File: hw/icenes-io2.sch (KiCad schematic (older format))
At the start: 35 parts, among them J4 Conn_02x31_Odd_Even, J5 Conn_02x31_Odd_Even, U4 iCE40HX8K-CT256, X2 DSC1001BI2-133.0000T

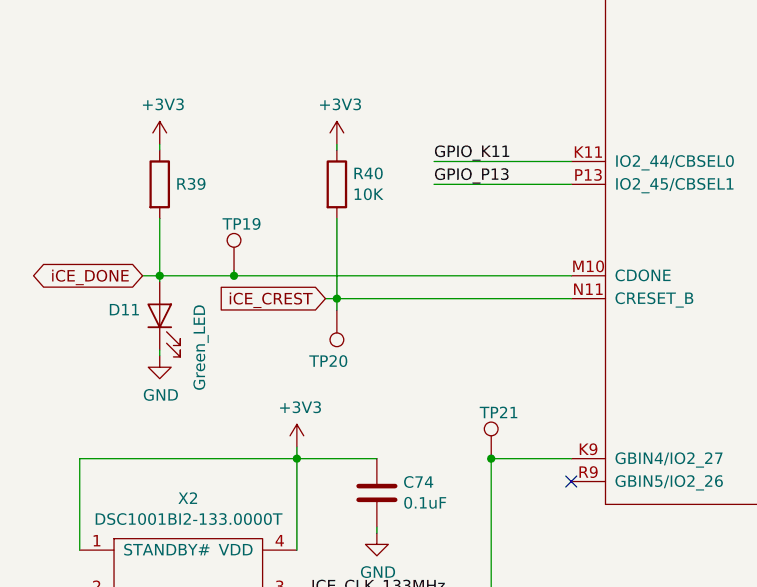
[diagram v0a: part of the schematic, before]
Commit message: Added voltage range in Vin lable (+5V to +10V).
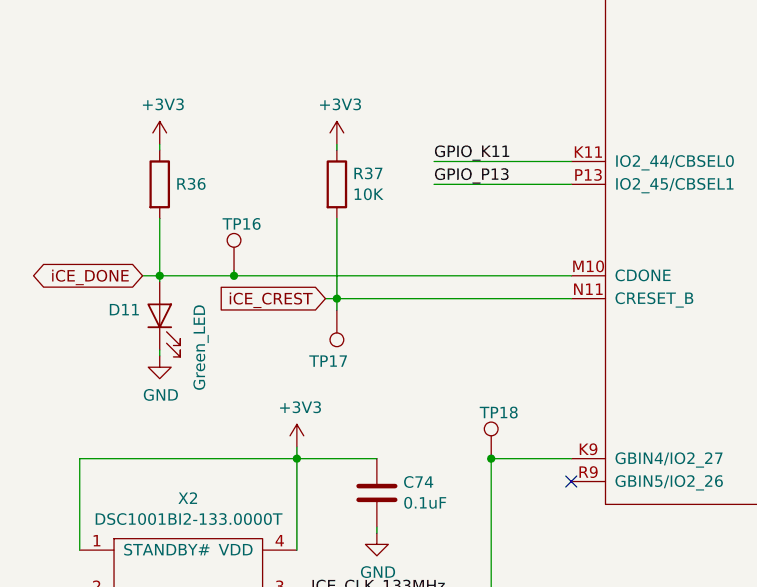
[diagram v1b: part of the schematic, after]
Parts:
- renumbered R39 to R36, R40 to R37, TP19 to TP16, TP20 to TP17, TP21 to TP18
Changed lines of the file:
@@
 $EndComp
 $Comp
-L icenes-library:R10K R40
+L icenes-library:R10K R37
 U 1 1 5D1F5A80
 P 2075 4200
-F 0 "R40" V 2029 4270 50  0000 L CNN
+F 0 "R37" V 2029 4270 50  0000 L CNN
 F 1 "R10K" H 2075 4100 50  0001 C CNN
 F 2 "Resistor_SMD:R_0603_1608Metric_Pad1.05x0.95mm_HandSolder" V 2075 4200 50  0001 C CNN
@@
 NoConn ~ 9850 6300
 $Comp
-L icenes-library:R_TBD R39
+L icenes-library:R_TBD R36
 U 1 1 5DA26BEC
 P 1300 4200
-F 0 "R39" V 1300 4270 50  0000 L CNN
+F 0 "R36" V 1300 4270 50  0000 L CNN
 F 1 "R_TBD" H 1300 4100 50  0001 C CNN
 F 2 "Resistor_SMD:R_0603_1608Metric_Pad1.05x0.95mm_HandSolder" V 1300 4200 50  0001 C CNN
@@
 	1300 4350 1300 4600
 $Comp
-L icenes-library:TestPoint TP20
+L icenes-library:TestPoint TP17
 U 1 1 5DCF35FF
 P 2075 4750
-F 0 "TP20" H 2025 4975 50  0000 L CNN
+F 0 "TP17" H 2025 4975 50  0000 L CNN
 F 1 "TestPoint" H 2075 4950 50  0001 C CNN
 F 2 "TestPoint:TestPoint_Pad_D1.0mm" H 2275 4750 50  0001 C CNN
@@
 	2250 5725 2250 5700
 $Comp
-L icenes-library:TestPoint TP21
+L icenes-library:TestPoint TP18
 U 1 1 5DDBB4BD
 P 2750 5400
-F 0 "TP21" H 2700 5600 50  0000 L CNN
+F 0 "TP18" H 2700 5600 50  0000 L CNN
 F 1 "TestPoint" H 2750 5600 50  0001 C CNN
 F 2 "TestPoint:TestPoint_Pad_D1.0mm" H 2950 5400 50  0001 C CNN
@@
 $EndComp
 $Comp
-L icenes-library:TestPoint TP19
+L icenes-library:TestPoint TP16
 U 1 1 5DDC0B2C
 P 1625 4575
-F 0 "TP19" H 1575 4775 50  0000 L CNN
+F 0 "TP16" H 1575 4775 50  0000 L CNN
 F 1 "TestPoint" H 1625 4775 50  0001 C CNN
 F 2 "TestPoint:TestPoint_Pad_D1.0mm" H 1825 4575 50  0001 C CNN

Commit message: Rough board layout.
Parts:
- added R38: R0_0603, Resistor_SMD:R_0603_1608Metric_Pad1.05x0.95mm_HandSolder, symbol icenes-library:R0_0603
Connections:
- net iCE_DONE: now also R38.1; no longer D11.2 (A)
- new net: D11.2 (A), R38.2
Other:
- moved on the sheet: C74, D11, X2
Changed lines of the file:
@@
 L icenes-library:Green_LED D11
 U 1 1 5DA2730F
-P 1300 4775
-F 0 "D11" V 1325 5000 50  0000 R CNN
-F 1 "Green_LED" H 1350 4600 50  0000 R CNN
-F 2 "LED_SMD:LED_0805_2012Metric_Pad1.15x1.40mm_HandSolder" H 1300 4775 50  0001 C CNN
-F 3 "https://www.mouser.se/datasheet/2/216/APTD2012LCGCK-1102037.pdf" H 1300 4775 50  0001 C CNN
-F 4 "Kingbright" H 1300 4775 50  0001 C CNN "Manufacturer"
-F 5 "APTD2012LCGCK" H 1300 4775 50  0001 C CNN "Part number"
-	1    1300 4775
+P 1300 5100
+F 0 "D11" V 1325 5325 50  0000 R CNN
+F 1 "Green_LED" H 1350 4925 50  0000 R CNN
+F 2 "LED_SMD:LED_0805_2012Metric_Pad1.15x1.40mm_HandSolder" H 1300 5100 50  0001 C CNN
+F 3 "https://www.mouser.se/datasheet/2/216/APTD2012LCGCK-1102037.pdf" H 1300 5100 50  0001 C CNN
+F 4 "Kingbright" H 1300 5100 50  0001 C CNN "Manufacturer"
+F 5 "APTD2012LCGCK" H 1300 5100 50  0001 C CNN "Part number"
+	1    1300 5100
 	0    -1   -1   0
 $EndComp
@@
 L power:GND #PWR?
 U 1 1 5DA5244F
-P 1300 4950
+P 1300 5275
 AR Path="/5D1BB1FB/5DA5244F" Ref="#PWR?"  Part="1"
 AR Path="/5D1BB49B/5DA5244F" Ref="#PWR090"  Part="1"
-F 0 "#PWR090" H 1300 4700 50  0001 C CNN
-F 1 "GND" H 1305 4777 50  0000 C CNN
-F 2 "" H 1300 4950 50  0001 C CNN
-F 3 "" H 1300 4950 50  0001 C CNN
-	1    1300 4950
+F 0 "#PWR090" H 1300 5025 50  0001 C CNN
+F 1 "GND" H 1305 5102 50  0000 C CNN
+F 2 "" H 1300 5275 50  0001 C CNN
+F 3 "" H 1300 5275 50  0001 C CNN
+	1    1300 5275
 	1    0    0    -1
 $EndComp
@@
 	1300 4025 1300 4050
 Wire Wire Line
-	1300 4925 1300 4950
+	1300 5250 1300 5275
 Wire Wire Line
 	1225 4600 1300 4600
@@
 L icenes-library:C0.1uF C?
 U 1 1 5DC56E81
-P 2250 5550
+P 2250 5650
 AR Path="/5D1BAC88/5DC56E81" Ref="C?"  Part="1"
 AR Path="/5D1BB49B/5DC56E81" Ref="C74"  Part="1"
-F 0 "C74" H 2365 5596 50  0000 L CNN
-F 1 "C0.1uF" H 2100 5450 50  0001 C CNN
-F 2 "Capacitor_SMD:C_0603_1608Metric_Pad1.05x0.95mm_HandSolder" H 2250 5550 50  0001 C CNN
-F 3 "https://www.mouser.se/datasheet/2/445/885012206020-554242.pdf" H 2250 5550 50  0001 C CNN
-F 4 "0.1uF" H 2365 5505 50  0000 L CNN "Capacitance"
-F 5 "Wurth" H 2250 5550 50  0001 C CNN "Manufacturer"
-F 6 "885012206020 " H 2250 5550 50  0001 C CNN "Part number"
-	1    2250 5550
+F 0 "C74" H 2365 5696 50  0000 L CNN
+F 1 "C0.1uF" H 2100 5550 50  0001 C CNN
+F 2 "Capacitor_SMD:C_0603_1608Metric_Pad1.05x0.95mm_HandSolder" H 2250 5650 50  0001 C CNN
+F 3 "https://www.mouser.se/datasheet/2/445/885012206020-554242.pdf" H 2250 5650 50  0001 C CNN
+F 4 "0.1uF" H 2365 5605 50  0000 L CNN "Capacitance"
+F 5 "Wurth" H 2250 5650 50  0001 C CNN "Manufacturer"
+F 6 "885012206020 " H 2250 5650 50  0001 C CNN "Part number"
+	1    2250 5650
 	1    0    0    -1
 $EndComp
@@
 L power:GND #PWR?
 U 1 1 5DC56E8F
-P 2250 5725
+P 2250 5825
 AR Path="/5D1BAC88/5DC56E8F" Ref="#PWR?"  Part="1"
 AR Path="/5D1BB49B/5DC56E8F" Ref="#PWR0104"  Part="1"
-F 0 "#PWR0104" H 2250 5475 50  0001 C CNN
-F 1 "GND" H 2255 5552 50  0000 C CNN
-F 2 "" H 2250 5725 50  0001 C CNN
-F 3 "" H 2250 5725 50  0001 C CNN
-	1    2250 5725
-	1    0    0    -1
-$EndComp
-Wire Wire Line
-	1900 5400 2250 5400
-Wire Wire Line
-	1900 5400 1900 5800
-Wire Wire Line
-	1900 5350 1900 5400
-Connection ~ 1900 5400
-Wire Wire Line
-	950  5800 950  5400
-Wire Wire Line
-	950  5400 1900 5400
+F 0 "#PWR0104" H 2250 5575 50  0001 C CNN
+F 1 "GND" H 2255 5652 50  0000 C CNN
+F 2 "" H 2250 5825 50  0001 C CNN
+F 3 "" H 2250 5825 50  0001 C CNN
+	1    2250 5825
+	1    0    0    -1
+$EndComp
+Wire Wire Line
+	1900 5500 2250 5500
+Wire Wire Line
+	1900 5500 1900 5900
+Wire Wire Line
+	1900 5450 1900 5500
+Connection ~ 1900 5500
+Wire Wire Line
+	950  5900 950  5500
+Wire Wire Line
+	950  5500 1900 5500
 $Comp
 L power:GND #PWR?
 U 1 1 5DC56E9C
-P 950 6100
+P 950 6200
 AR Path="/5D1BAC88/5DC56E9C" Ref="#PWR?"  Part="1"
 AR Path="/5D1BB49B/5DC56E9C" Ref="#PWR087"  Part="1"
-F 0 "#PWR087" H 950 5850 50  0001 C CNN
-F 1 "GND" H 955 5927 50  0000 C CNN
-F 2 "" H 950 6100 50  0001 C CNN
-F 3 "" H 950 6100 50  0001 C CNN
-	1    950  6100
-	1    0    0    -1
-$EndComp
-Wire Wire Line
-	950  6000 950  6100
-Wire Wire Line
-	1900 6000 2750 6000
+F 0 "#PWR087" H 950 5950 50  0001 C CNN
+F 1 "GND" H 955 6027 50  0000 C CNN
+F 2 "" H 950 6200 50  0001 C CNN
+F 3 "" H 950 6200 50  0001 C CNN
+	1    950  6200
+	1    0    0    -1
+$EndComp
+Wire Wire Line
+	950  6100 950  6200
+Wire Wire Line
+	1900 6100 2750 6100
 $Comp
 L icenes-library:DSC1001BI2-133.0000T X2
 U 1 1 5DCE10E2
-P 1450 5700
-F 0 "X2" H 1425 5825 50  0000 C CNN
-F 1 "DSC1001BI2-133.0000T" H 1425 5734 50  0000 C CNN
-F 2 "icenes-library:MEMS_Microship_Ocillator_SMD_CDFN-4_5.0x3.2mm" H 1550 5750 50  0001 C CNN
-F 3 "https://ww1.microchip.com/downloads/en/DeviceDoc/20005529B.pdf" H 1550 5750 50  0001 C CNN
-F 4 "Microchip" H 1450 5700 50  0001 C CNN "Manufacturer"
-F 5 "DSC1001BI2-133.0000T" H 1450 5700 50  0001 C CNN "Part number"
-	1    1450 5700
-	1    0    0    -1
-$EndComp
-Wire Wire Line
-	2750 6000 2750 5400
+P 1450 5800
+F 0 "X2" H 1425 5925 50  0000 C CNN
+F 1 "DSC1001BI2-133.0000T" H 1425 5834 50  0000 C CNN
+F 2 "icenes-library:MEMS_Microship_Ocillator_SMD_CDFN-4_5.0x3.2mm" H 1550 5850 50  0001 C CNN
+F 3 "https://ww1.microchip.com/downloads/en/DeviceDoc/20005529B.pdf" H 1550 5850 50  0001 C CNN
+F 4 "Microchip" H 1450 5800 50  0001 C CNN "Manufacturer"
+F 5 "DSC1001BI2-133.0000T" H 1450 5800 50  0001 C CNN "Part number"
+	1    1450 5800
+	1    0    0    -1
+$EndComp
 Wire Wire Line
 	2750 5400 3100 5400
 NoConn ~ 3100 5500
-Text Label 2550 6000 2    50   ~ 0
+Text Label 2550 6100 2    50   ~ 0
 ICE_CLK_133MHz
 Wire Wire Line
-	2250 5725 2250 5700
+	2250 5825 2250 5800
 $Comp
 L icenes-library:TestPoint TP18
@@
 L power:+3V3 #PWR095
 U 1 1 5DDBDDE4
-P 1900 5350
-F 0 "#PWR095" H 1900 5200 50  0001 C CNN
-F 1 "+3V3" H 1915 5523 50  0000 C CNN
-F 2 "" H 1900 5350 50  0001 C CNN
-F 3 "" H 1900 5350 50  0001 C CNN
-	1    1900 5350
+P 1900 5450
+F 0 "#PWR095" H 1900 5300 50  0001 C CNN
+F 1 "+3V3" H 1915 5623 50  0000 C CNN
+F 2 "" H 1900 5450 50  0001 C CNN
+F 3 "" H 1900 5450 50  0001 C CNN
+	1    1900 5450
 	1    0    0    -1
 $EndComp
@@
 Wire Wire Line
 	2550 3000 2550 3050
+$Comp
+L icenes-library:R0_0603 R38
+U 1 1 5DCDC52E
+P 1300 4775
+F 0 "R38" V 1254 4845 50  0000 L CNN
+F 1 "R0_0603" H 1300 4675 50  0001 C CNN
+F 2 "Resistor_SMD:R_0603_1608Metric_Pad1.05x0.95mm_HandSolder" V 1300 4775 50  0001 C CNN
+F 3 "https://www.mouser.se/datasheet/2/447/PYu-RC_Group_51_RoHS_L_10-1527934.pdf" V 1300 4775 50  0001 C CNN
+F 4 "0" V 1345 4845 50  0000 L CNN "Resistance"
+F 5 "Yageo" H 1300 4775 50  0001 C CNN "Manufacturer"
+F 6 "RC0603FR-070RL" H 1300 4775 50  0001 C CNN "Part number"
+	1    1300 4775
+	0    1    1    0
+$EndComp
+Wire Wire Line
+	1300 4925 1300 4950
+Wire Wire Line
+	2750 5400 2750 6100
 $EndSCHEMATC

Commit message: Layout.
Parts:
- removed C74: C0.1uF, Capacitor_SMD:C_0603_1608Metric_Pad1.05x0.95mm_HandSolder, symbol icenes-library:C0.1uF
- removed D11: Green_LED, LED_SMD:LED_0805_2012Metric_Pad1.15x1.40mm_HandSolder, symbol icenes-library:Green_LED
- removed R38: R0_0603, Resistor_SMD:R_0603_1608Metric_Pad1.05x0.95mm_HandSolder, symbol icenes-library:R0_0603
- removed TP18: TestPoint, TestPoint:TestPoint_Pad_D1.0mm, symbol icenes-library:TestPoint
- removed X2: DSC1001BI2-133.0000T, icenes-library:MEMS_Microship_Ocillator_SMD_CDFN-4_5.0x3.2mm, symbol icenes-library:DSC1001BI2-133.0000T
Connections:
- net ICE_CLK_133MHz: no longer names the net of U4.K9 (GBIN4/IO2_27)
- no-connect marks 2 -> 3
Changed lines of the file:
@@
-$EndComp
-$Comp
-L icenes-library:Green_LED D11
-U 1 1 5DA2730F
-P 1300 5100
-F 0 "D11" V 1325 5325 50  0000 R CNN
-F 1 "Green_LED" H 1350 4925 50  0000 R CNN
-F 2 "LED_SMD:LED_0805_2012Metric_Pad1.15x1.40mm_HandSolder" H 1300 5100 50  0001 C CNN
-F 3 "https://www.mouser.se/datasheet/2/216/APTD2012LCGCK-1102037.pdf" H 1300 5100 50  0001 C CNN
-F 4 "Kingbright" H 1300 5100 50  0001 C CNN "Manufacturer"
-F 5 "APTD2012LCGCK" H 1300 5100 50  0001 C CNN "Part number"
-	1    1300 5100
-	0    -1   -1   0
 $EndComp
 $Comp
@@
 	1    0    0    -1
 $EndComp
-$Comp
-L power:GND #PWR?
-U 1 1 5DA5244F
-P 1300 5275
-AR Path="/5D1BB1FB/5DA5244F" Ref="#PWR?"  Part="1"
-AR Path="/5D1BB49B/5DA5244F" Ref="#PWR090"  Part="1"
-F 0 "#PWR090" H 1300 5025 50  0001 C CNN
-F 1 "GND" H 1305 5102 50  0000 C CNN
-F 2 "" H 1300 5275 50  0001 C CNN
-F 3 "" H 1300 5275 50  0001 C CNN
-	1    1300 5275
-	1    0    0    -1
-$EndComp
 Wire Wire Line
 	1300 4025 1300 4050
 Wire Wire Line
-	1300 5250 1300 5275
-Wire Wire Line
 	1225 4600 1300 4600
 Connection ~ 1300 4600
-Wire Wire Line
-	1300 4600 1300 4625
 Wire Wire Line
 	1300 4600 1625 4600
@@
 Wire Wire Line
 	2075 4750 2075 4700
-$Comp
-L icenes-library:C0.1uF C?
-U 1 1 5DC56E81
-P 2250 5650
-AR Path="/5D1BAC88/5DC56E81" Ref="C?"  Part="1"
-AR Path="/5D1BB49B/5DC56E81" Ref="C74"  Part="1"
-F 0 "C74" H 2365 5696 50  0000 L CNN
-F 1 "C0.1uF" H 2100 5550 50  0001 C CNN
-F 2 "Capacitor_SMD:C_0603_1608Metric_Pad1.05x0.95mm_HandSolder" H 2250 5650 50  0001 C CNN
-F 3 "https://www.mouser.se/datasheet/2/445/885012206020-554242.pdf" H 2250 5650 50  0001 C CNN
-F 4 "0.1uF" H 2365 5605 50  0000 L CNN "Capacitance"
-F 5 "Wurth" H 2250 5650 50  0001 C CNN "Manufacturer"
-F 6 "885012206020 " H 2250 5650 50  0001 C CNN "Part number"
-	1    2250 5650
-	1    0    0    -1
-$EndComp
-$Comp
-L power:GND #PWR?
-U 1 1 5DC56E8F
-P 2250 5825
-AR Path="/5D1BAC88/5DC56E8F" Ref="#PWR?"  Part="1"
-AR Path="/5D1BB49B/5DC56E8F" Ref="#PWR0104"  Part="1"
-F 0 "#PWR0104" H 2250 5575 50  0001 C CNN
-F 1 "GND" H 2255 5652 50  0000 C CNN
-F 2 "" H 2250 5825 50  0001 C CNN
-F 3 "" H 2250 5825 50  0001 C CNN
-	1    2250 5825
-	1    0    0    -1
-$EndComp
-Wire Wire Line
-	1900 5500 2250 5500
-Wire Wire Line
-	1900 5500 1900 5900
-Wire Wire Line
-	1900 5450 1900 5500
-Connection ~ 1900 5500
-Wire Wire Line
-	950  5900 950  5500
-Wire Wire Line
-	950  5500 1900 5500
-$Comp
-L power:GND #PWR?
-U 1 1 5DC56E9C
-P 950 6200
-AR Path="/5D1BAC88/5DC56E9C" Ref="#PWR?"  Part="1"
-AR Path="/5D1BB49B/5DC56E9C" Ref="#PWR087"  Part="1"
-F 0 "#PWR087" H 950 5950 50  0001 C CNN
-F 1 "GND" H 955 6027 50  0000 C CNN
-F 2 "" H 950 6200 50  0001 C CNN
-F 3 "" H 950 6200 50  0001 C CNN
-	1    950  6200
-	1    0    0    -1
-$EndComp
-Wire Wire Line
-	950  6100 950  6200
-Wire Wire Line
-	1900 6100 2750 6100
-$Comp
-L icenes-library:DSC1001BI2-133.0000T X2
-U 1 1 5DCE10E2
-P 1450 5800
-F 0 "X2" H 1425 5925 50  0000 C CNN
-F 1 "DSC1001BI2-133.0000T" H 1425 5834 50  0000 C CNN
-F 2 "icenes-library:MEMS_Microship_Ocillator_SMD_CDFN-4_5.0x3.2mm" H 1550 5850 50  0001 C CNN
-F 3 "https://www.mouser.se/datasheet/2/268/20005529A-1149183.pdf" H 1550 5850 50  0001 C CNN
-F 4 "Microchip" H 1450 5800 50  0001 C CNN "Manufacturer"
-F 5 "DSC1001BI2-133.0000T" H 1450 5800 50  0001 C CNN "Part number"
-	1    1450 5800
-	1    0    0    -1
-$EndComp
-Wire Wire Line
-	2750 5400 3100 5400
 NoConn ~ 3100 5500
-Text Label 2550 6100 2    50   ~ 0
-ICE_CLK_133MHz
-Wire Wire Line
-	2250 5825 2250 5800
-$Comp
-L icenes-library:TestPoint TP18
-U 1 1 5DDBB4BD
-P 2750 5400
-F 0 "TP18" H 2700 5600 50  0000 L CNN
-F 1 "TestPoint" H 2750 5600 50  0001 C CNN
-F 2 "TestPoint:TestPoint_Pad_D1.0mm" H 2950 5400 50  0001 C CNN
-F 3 "~" H 2950 5400 50  0001 C CNN
-	1    2750 5400
-	1    0    0    -1
-$EndComp
-Connection ~ 2750 5400
-$Comp
-L power:+3V3 #PWR095
-U 1 1 5DDBDDE4
-P 1900 5450
-F 0 "#PWR095" H 1900 5300 50  0001 C CNN
-F 1 "+3V3" H 1915 5623 50  0000 C CNN
-F 2 "" H 1900 5450 50  0001 C CNN
-F 3 "" H 1900 5450 50  0001 C CNN
-	1    1900 5450
-	1    0    0    -1
-$EndComp
 $Comp
 L icenes-library:TestPoint TP16
@@
 Wire Wire Line
 	2550 3000 2550 3050
-$Comp
-L icenes-library:R0_0603 R38
-U 1 1 5DCDC52E
-P 1300 4775
-F 0 "R38" V 1254 4845 50  0000 L CNN
-F 1 "R0_0603" H 1300 4675 50  0001 C CNN
-F 2 "Resistor_SMD:R_0603_1608Metric_Pad1.05x0.95mm_HandSolder" V 1300 4775 50  0001 C CNN
-F 3 "https://www.mouser.se/datasheet/2/447/PYu-RC_Group_51_RoHS_L_10-1527934.pdf" V 1300 4775 50  0001 C CNN
-F 4 "0" V 1345 4845 50  0000 L CNN "Resistance"
-F 5 "Yageo" H 1300 4775 50  0001 C CNN "Manufacturer"
-F 6 "RC0603FR-070RL" H 1300 4775 50  0001 C CNN "Part number"
-	1    1300 4775
-	0    1    1    0
-$EndComp
-Wire Wire Line
-	1300 4925 1300 4950
-Wire Wire Line
-	2750 5400 2750 6100
+NoConn ~ 3100 5400
 $EndSCHEMATC

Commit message: Layout.
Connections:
- net +1V2: now also C66.1, C67.2, C80.1, C81.2, J4.5 (Pin_5), J4.57 (Pin_57), J5.5 (Pin_5), J5.57 (Pin_57); no longer C77.1, C78.2, C88.1, C89.2, J4.1 (Pin_1), J4.61 (Pin_61), J5.1 (Pin_1), J5.61 (Pin_61)
- net +5V: now also C77.1, C78.2, C88.1, C89.2, J4.1 (Pin_1), J4.61 (Pin_61), J5.1 (Pin_1), J5.61 (Pin_61); no longer C66.1, C67.2, C80.1, C81.2, J4.5 (Pin_5), J4.57 (Pin_57), J5.5 (Pin_5), J5.57 (Pin_57)
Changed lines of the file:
@@
 L power:+1V2 #PWR?
 U 1 1 5D56D351
-P 2550 6775
+P 1600 6775
 AR Path="/5D1BB1FB/5D56D351" Ref="#PWR?"  Part="1"
 AR Path="/5D1BB49B/5D56D351" Ref="#PWR0106"  Part="1"
-F 0 "#PWR0106" H 2550 6625 50  0001 C CNN
-F 1 "+1V2" H 2565 6948 50  0000 C CNN
+F 0 "#PWR0106" H 1600 6625 50  0001 C CNN
+F 1 "+1V2" H 1615 6948 50  0000 C CNN
+F 2 "" H 1600 6775 50  0001 C CNN
+F 3 "" H 1600 6775 50  0001 C CNN
+	1    1600 6775
+	1    0    0    -1
+$EndComp
+$Comp
+L power:+5V #PWR?
+U 1 1 5D56D357
+P 2550 6775
+AR Path="/5D1BB1FB/5D56D357" Ref="#PWR?"  Part="1"
+AR Path="/5D1BB49B/5D56D357" Ref="#PWR091"  Part="1"
+F 0 "#PWR091" H 2550 6625 50  0001 C CNN
+F 1 "+5V" H 2565 6948 50  0000 C CNN
 F 2 "" H 2550 6775 50  0001 C CNN
 F 3 "" H 2550 6775 50  0001 C CNN
 	1    2550 6775
-	1    0    0    -1
-$EndComp
-$Comp
-L power:+5V #PWR?
-U 1 1 5D56D357
-P 1600 6775
-AR Path="/5D1BB1FB/5D56D357" Ref="#PWR?"  Part="1"
-AR Path="/5D1BB49B/5D56D357" Ref="#PWR091"  Part="1"
-F 0 "#PWR091" H 1600 6625 50  0001 C CNN
-F 1 "+5V" H 1615 6948 50  0000 C CNN
-F 2 "" H 1600 6775 50  0001 C CNN
-F 3 "" H 1600 6775 50  0001 C CNN
-	1    1600 6775
 	1    0    0    -1
 $EndComp
@@
 L power:+1V2 #PWR?
 U 1 1 5D590B47
-P 2550 10425
+P 1600 10425
 AR Path="/5D1BB1FB/5D590B47" Ref="#PWR?"  Part="1"
 AR Path="/5D1BB49B/5D590B47" Ref="#PWR0108"  Part="1"
-F 0 "#PWR0108" H 2550 10275 50  0001 C CNN
-F 1 "+1V2" H 2565 10598 50  0000 C CNN
+F 0 "#PWR0108" H 1600 10275 50  0001 C CNN
+F 1 "+1V2" H 1615 10598 50  0000 C CNN
+F 2 "" H 1600 10425 50  0001 C CNN
+F 3 "" H 1600 10425 50  0001 C CNN
+	1    1600 10425
+	-1   0    0    -1
+$EndComp
+$Comp
+L power:+5V #PWR?
+U 1 1 5D590B4D
+P 2550 10425
+AR Path="/5D1BB1FB/5D590B4D" Ref="#PWR?"  Part="1"
+AR Path="/5D1BB49B/5D590B4D" Ref="#PWR093"  Part="1"
+F 0 "#PWR093" H 2550 10275 50  0001 C CNN
+F 1 "+5V" H 2565 10598 50  0000 C CNN
 F 2 "" H 2550 10425 50  0001 C CNN
 F 3 "" H 2550 10425 50  0001 C CNN
 	1    2550 10425
-	-1   0    0    -1
-$EndComp
-$Comp
-L power:+5V #PWR?
-U 1 1 5D590B4D
-P 1600 10425
-AR Path="/5D1BB1FB/5D590B4D" Ref="#PWR?"  Part="1"
-AR Path="/5D1BB49B/5D590B4D" Ref="#PWR093"  Part="1"
-F 0 "#PWR093" H 1600 10275 50  0001 C CNN
-F 1 "+5V" H 1615 10598 50  0000 C CNN
-F 2 "" H 1600 10425 50  0001 C CNN
-F 3 "" H 1600 10425 50  0001 C CNN
-	1    1600 10425
 	-1   0    0    -1
 $EndComp
@@
 L power:+1V2 #PWR?
 U 1 1 5D78DE9E
-P 9300 6775
+P 8350 6775
 AR Path="/5D1BB1FB/5D78DE9E" Ref="#PWR?"  Part="1"
 AR Path="/5D1BB49B/5D78DE9E" Ref="#PWR0125"  Part="1"
-F 0 "#PWR0125" H 9300 6625 50  0001 C CNN
-F 1 "+1V2" H 9315 6948 50  0000 C CNN
+F 0 "#PWR0125" H 8350 6625 50  0001 C CNN
+F 1 "+1V2" H 8365 6948 50  0000 C CNN
+F 2 "" H 8350 6775 50  0001 C CNN
+F 3 "" H 8350 6775 50  0001 C CNN
+	1    8350 6775
+	1    0    0    -1
+$EndComp
+$Comp
+L power:+5V #PWR?
+U 1 1 5D78DEA4
+P 9300 6775
+AR Path="/5D1BB1FB/5D78DEA4" Ref="#PWR?"  Part="1"
+AR Path="/5D1BB49B/5D78DEA4" Ref="#PWR0114"  Part="1"
+F 0 "#PWR0114" H 9300 6625 50  0001 C CNN
+F 1 "+5V" H 9315 6948 50  0000 C CNN
 F 2 "" H 9300 6775 50  0001 C CNN
 F 3 "" H 9300 6775 50  0001 C CNN
 	1    9300 6775
-	1    0    0    -1
-$EndComp
-$Comp
-L power:+5V #PWR?
-U 1 1 5D78DEA4
-P 8350 6775
-AR Path="/5D1BB1FB/5D78DEA4" Ref="#PWR?"  Part="1"
-AR Path="/5D1BB49B/5D78DEA4" Ref="#PWR0114"  Part="1"
-F 0 "#PWR0114" H 8350 6625 50  0001 C CNN
-F 1 "+5V" H 8365 6948 50  0000 C CNN
-F 2 "" H 8350 6775 50  0001 C CNN
-F 3 "" H 8350 6775 50  0001 C CNN
-	1    8350 6775
 	1    0    0    -1
 $EndComp
@@
 L power:+1V2 #PWR?
 U 1 1 5D78DEEF
-P 9300 10425
+P 8350 10425
 AR Path="/5D1BB1FB/5D78DEEF" Ref="#PWR?"  Part="1"
 AR Path="/5D1BB49B/5D78DEEF" Ref="#PWR0127"  Part="1"
-F 0 "#PWR0127" H 9300 10275 50  0001 C CNN
-F 1 "+1V2" H 9315 10598 50  0000 C CNN
+F 0 "#PWR0127" H 8350 10275 50  0001 C CNN
+F 1 "+1V2" H 8365 10598 50  0000 C CNN
+F 2 "" H 8350 10425 50  0001 C CNN
+F 3 "" H 8350 10425 50  0001 C CNN
+	1    8350 10425
+	-1   0    0    -1
+$EndComp
+$Comp
+L power:+5V #PWR?
+U 1 1 5D78DEF5
+P 9300 10425
+AR Path="/5D1BB1FB/5D78DEF5" Ref="#PWR?"  Part="1"
+AR Path="/5D1BB49B/5D78DEF5" Ref="#PWR0116"  Part="1"
+F 0 "#PWR0116" H 9300 10275 50  0001 C CNN
+F 1 "+5V" H 9315 10598 50  0000 C CNN
 F 2 "" H 9300 10425 50  0001 C CNN
 F 3 "" H 9300 10425 50  0001 C CNN
 	1    9300 10425
-	-1   0    0    -1
-$EndComp
-$Comp
-L power:+5V #PWR?
-U 1 1 5D78DEF5
-P 8350 10425
-AR Path="/5D1BB1FB/5D78DEF5" Ref="#PWR?"  Part="1"
-AR Path="/5D1BB49B/5D78DEF5" Ref="#PWR0116"  Part="1"
-F 0 "#PWR0116" H 8350 10275 50  0001 C CNN
-F 1 "+5V" H 8365 10598 50  0000 C CNN
-F 2 "" H 8350 10425 50  0001 C CNN
-F 3 "" H 8350 10425 50  0001 C CNN
-	1    8350 10425
 	-1   0    0    -1
 $EndComp
@@
 	2550 3000 2550 3050
 NoConn ~ 3100 5400
+Text Label 8050 1400 0    50   ~ 0
+VCCIO3_3V3
+Text Label 1300 1400 0    50   ~ 0
+VCCIO2_3V3
+Text Label 2200 2600 0    50   ~ 0
+VCCPLL1_1V2
 $EndSCHEMATC

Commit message: Layout.
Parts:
- added C60, C62, C64: C10uF, Capacitor_SMD:C_0603_1608Metric_Pad1.05x0.95mm_HandSolder, symbol icenes-library:C10uF
- added J3: Conn_02x11_Odd_Even, Connector_PinSocket_2.54mm:PinSocket_2x11_P2.54mm_Vertical, symbol icenes-library:Conn_02x11_Odd_Even
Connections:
- net labels added: CTSn, DCDn, DSRn, DTRn, RS232_RX_TTL, RS232_TX_TTL, RTSn
- net labels removed: GPIO_N10, GPIO_N9, GPIO_P10, GPIO_P8, GPIO_P9, GPIO_R10, GPIO_T10
- wire segments 368 -> 407
